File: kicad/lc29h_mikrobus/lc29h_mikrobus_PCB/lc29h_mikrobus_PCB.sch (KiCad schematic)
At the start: 46 parts, among them IC1 MIKROE-924, IC101 DS28E36BQ+U, IC102 74LVC1G3157GV,125, J1 Conn_Coaxial, J2 Conn_01x03_Pin, Q1 DMP3013SFV, Q101 BC856B-13-F, Q102 BSS123L, Q3 BSS123L, Q4 PN2222A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

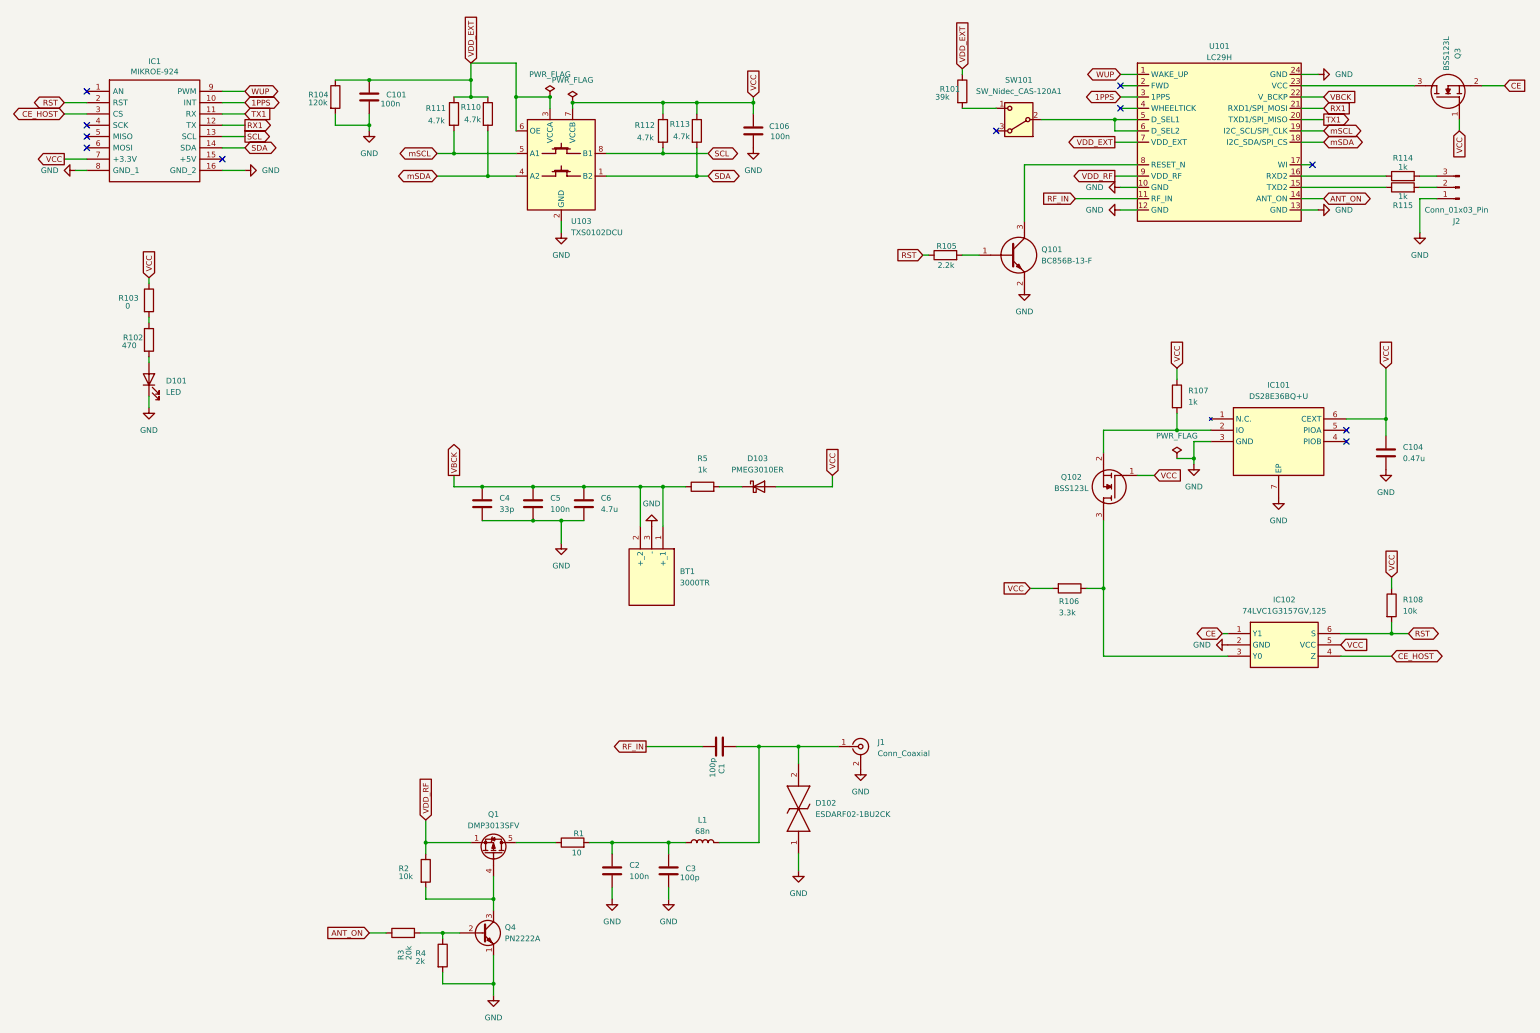
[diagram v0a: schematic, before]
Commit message: update schematic
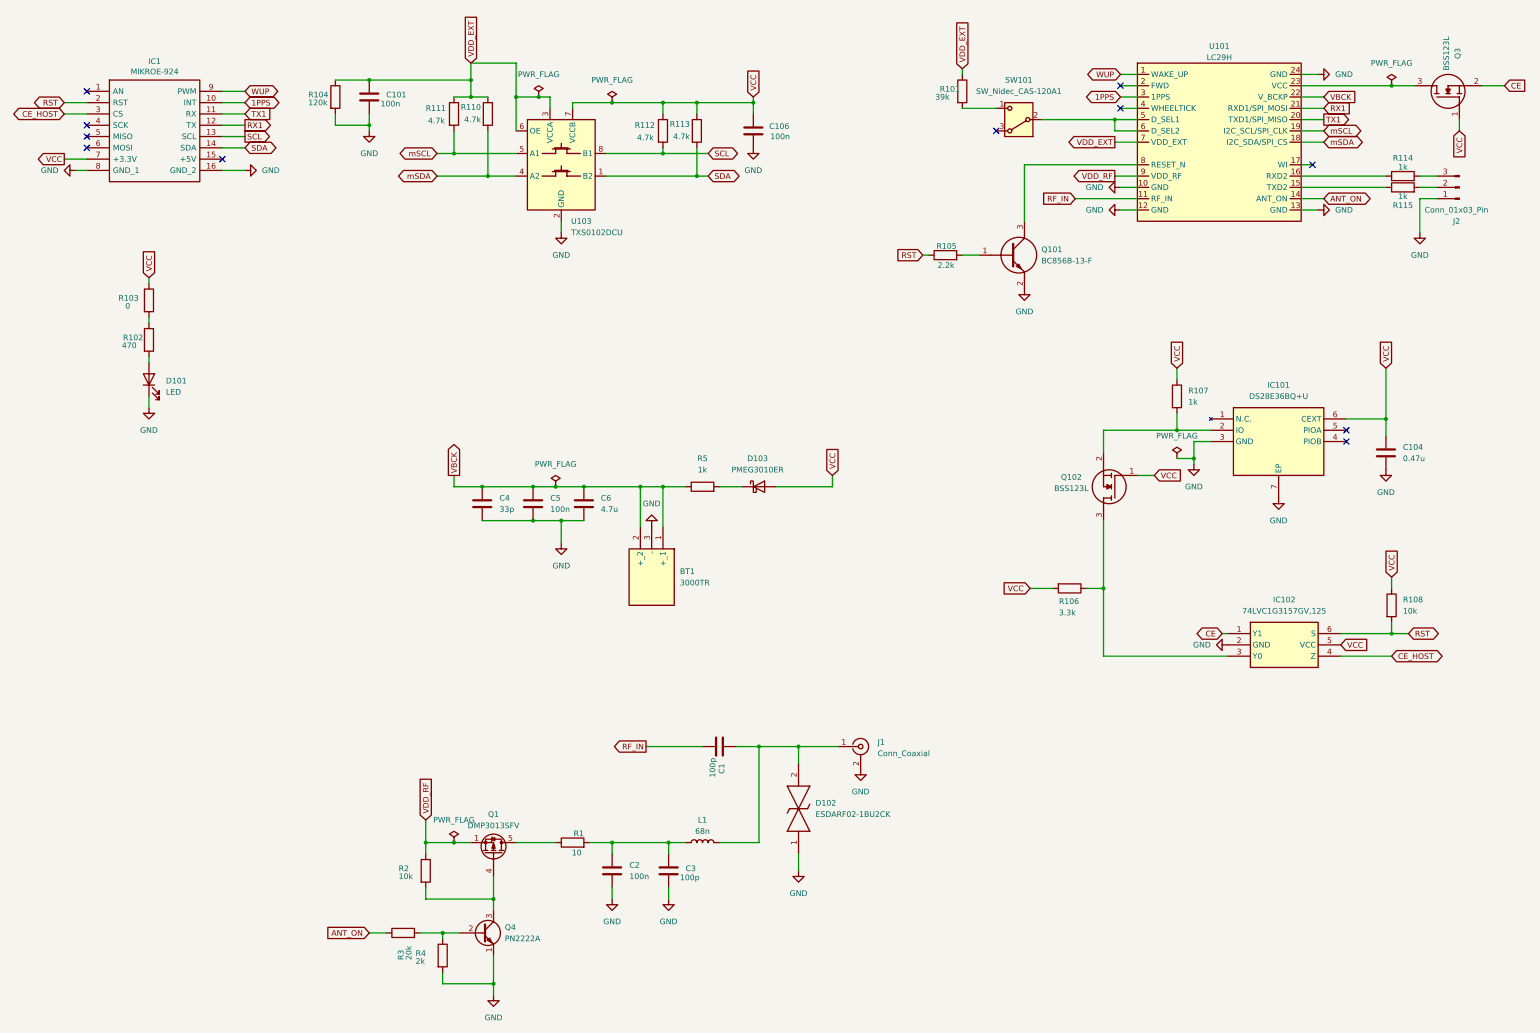
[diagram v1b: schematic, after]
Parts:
- IC1: footprint MIKROE-924:MIKROE924 -> MIKROE924; Description_1 (none) -> microSD click mikroBUS
